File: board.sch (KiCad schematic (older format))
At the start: 48 parts, among them J1 H3, J2 USB-UART, J3 H2, J4 H1, J5 PWR, J6 DL, J7 H4, Q1 Q_NPN_BCE, Q2 Q_NPN_BCE, SW1 RESET, U1 ASSoC, U2 LM1117-3.3, U3 LM1117-3.3, Y1 25 MHz

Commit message: Fix crystal's capacitor value, voltage regulator value. Improve overall placement.
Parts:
- C18: value 18n -> 18p
- U2: value LM1117-3.3 -> LM1117-1.8; symbol Regulator_Linear:LM1117-3.3 -> Regulator_Linear:LM1117-1.8
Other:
- note added: "1.8V LED"
- note added: "3.3V LED"
- note added: "External Memory"
- note added: "Power Access"
- note added: "Test Mode"
- note removed: "Extra Power Access"
- note removed: "Power LED (1.8v)"
- note removed: "Power LED (3.3v)"
- note removed: "Test Mode Switches"
- moved on the sheet: C17, C18, C19, D1, D2, J1, J3, J4, J6, J7, JP1, Q1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

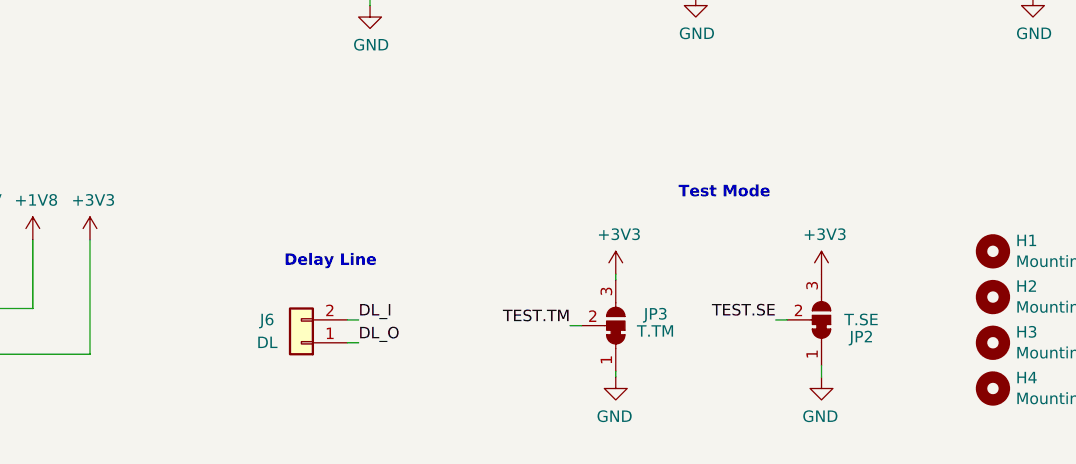
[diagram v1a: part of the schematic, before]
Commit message: Update using kicad 5.1.12
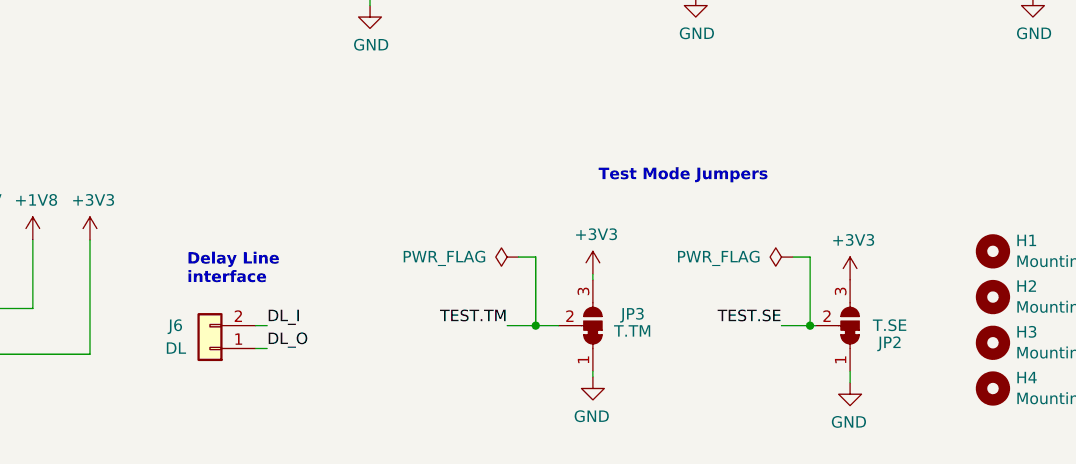
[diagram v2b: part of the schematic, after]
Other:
- note added: "Delay Line\ninterface"
- note added: "Test Mode Jumpers"
- note removed: "Delay Line"
- note removed: "Test Mode"
- moved on the sheet: J6, JP2, JP3
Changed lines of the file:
@@
 L Jumper:SolderJumper_3_Bridged12 JP3
 U 1 1 600FDD3B
-P 4450 7200
-F 0 "JP3" V 4500 7375 50  0000 C CNN
-F 1 "T.TM" V 4425 7375 50  0000 C CNN
-F 2 "Jumper:SolderJumper-3_P1.3mm_Bridged2Bar12_RoundedPad1.0x1.5mm" H 4450 7200 50  0001 C CNN
-F 3 "~" H 4450 7200 50  0001 C CNN
-	1    4450 7200
+P 4350 7200
+F 0 "JP3" V 4400 7375 50  0000 C CNN
+F 1 "T.TM" V 4325 7375 50  0000 C CNN
+F 2 "Jumper:SolderJumper-3_P1.3mm_Bridged2Bar12_RoundedPad1.0x1.5mm" H 4350 7200 50  0001 C CNN
+F 3 "~" H 4350 7200 50  0001 C CNN
+	1    4350 7200
 	0    1    -1   0
 $EndComp
@@
 L Jumper:SolderJumper_3_Bridged12 JP2
 U 1 1 6010189E
-P 5350 7175
-F 0 "JP2" V 5275 7350 50  0000 C CNN
-F 1 "T.SE" V 5350 7350 50  0000 C CNN
-F 2 "Jumper:SolderJumper-3_P1.3mm_Bridged2Bar12_RoundedPad1.0x1.5mm" H 5350 7175 50  0001 C CNN
-F 3 "~" H 5350 7175 50  0001 C CNN
-	1    5350 7175
+P 5475 7200
+F 0 "JP2" V 5400 7375 50  0000 C CNN
+F 1 "T.SE" V 5475 7375 50  0000 C CNN
+F 2 "Jumper:SolderJumper-3_P1.3mm_Bridged2Bar12_RoundedPad1.0x1.5mm" H 5475 7200 50  0001 C CNN
+F 3 "~" H 5475 7200 50  0001 C CNN
+	1    5475 7200
 	0    1    -1   0
 $EndComp
 Wire Wire Line
-	4450 7400 4450 7425
+	4350 7400 4350 7425
 $Comp
 L power:GND #PWR036
 U 1 1 60103E00
-P 4450 7425
-F 0 "#PWR036" H 4450 7175 50  0001 C CNN
-F 1 "GND" H 4455 7252 50  0000 C CNN
-F 2 "" H 4450 7425 50  0001 C CNN
-F 3 "" H 4450 7425 50  0001 C CNN
-	1    4450 7425
+P 4350 7425
+F 0 "#PWR036" H 4350 7175 50  0001 C CNN
+F 1 "GND" H 4355 7252 50  0000 C CNN
+F 2 "" H 4350 7425 50  0001 C CNN
+F 3 "" H 4350 7425 50  0001 C CNN
+	1    4350 7425
 	-1   0    0    -1
 $EndComp
@@
 L power:GND #PWR037
 U 1 1 6010E9C0
-P 5350 7425
-F 0 "#PWR037" H 5350 7175 50  0001 C CNN
-F 1 "GND" H 5355 7252 50  0000 C CNN
-F 2 "" H 5350 7425 50  0001 C CNN
-F 3 "" H 5350 7425 50  0001 C CNN
-	1    5350 7425
+P 5475 7450
+F 0 "#PWR037" H 5475 7200 50  0001 C CNN
+F 1 "GND" H 5480 7277 50  0000 C CNN
+F 2 "" H 5475 7450 50  0001 C CNN
+F 3 "" H 5475 7450 50  0001 C CNN
+	1    5475 7450
 	-1   0    0    -1
 $EndComp
@@
 L power:+3V3 #PWR034
 U 1 1 60137BAC
-P 4450 6975
-F 0 "#PWR034" H 4450 6825 50  0001 C CNN
-F 1 "+3V3" H 4465 7148 50  0000 C CNN
-F 2 "" H 4450 6975 50  0001 C CNN
-F 3 "" H 4450 6975 50  0001 C CNN
-	1    4450 6975
-	1    0    0    -1
-$EndComp
-Wire Wire Line
-	5350 7375 5350 7425
+P 4350 6975
+F 0 "#PWR034" H 4350 6825 50  0001 C CNN
+F 1 "+3V3" H 4365 7148 50  0000 C CNN
+F 2 "" H 4350 6975 50  0001 C CNN
+F 3 "" H 4350 6975 50  0001 C CNN
+	1    4350 6975
+	1    0    0    -1
+$EndComp
+Wire Wire Line
+	5475 7400 5475 7450
 $Comp
 L Connector_Generic:Conn_01x12 J1
@@
 L Connector_Generic:Conn_01x02 J6
 U 1 1 603C23F2
-P 3075 7275
-F 0 "J6" H 3225 7175 50  0000 C CNN
-F 1 "DL" H 3225 7275 50  0000 C CNN
-F 2 "Connector_PinSocket_2.54mm:PinSocket_1x02_P2.54mm_Vertical" H 3075 7275 50  0001 C CNN
-F 3 "~" H 3075 7275 50  0001 C CNN
-	1    3075 7275
+P 2675 7300
+F 0 "J6" H 2825 7200 50  0000 C CNN
+F 1 "DL" H 2825 7300 50  0000 C CNN
+F 2 "Connector_PinSocket_2.54mm:PinSocket_1x02_P2.54mm_Vertical" H 2675 7300 50  0001 C CNN
+F 3 "~" H 2675 7300 50  0001 C CNN
+	1    2675 7300
 	-1   0    0    1
 $EndComp
@@
 	8625 1475 8625 1525
 Wire Wire Line
-	4450 6975 4450 7000
+	4350 6975 4350 7000
 Text Label 9675 3075 0    50   ~ 0
 TEST.TM
@@
 L power:+3V3 #PWR035
 U 1 1 605DD584
-P 5350 6975
-F 0 "#PWR035" H 5350 6825 50  0001 C CNN
-F 1 "+3V3" H 5365 7148 50  0000 C CNN
-F 2 "" H 5350 6975 50  0001 C CNN
-F 3 "" H 5350 6975 50  0001 C CNN
-	1    5350 6975
+P 5475 7000
+F 0 "#PWR035" H 5475 6850 50  0001 C CNN
+F 1 "+3V3" H 5490 7173 50  0000 C CNN
+F 2 "" H 5475 7000 50  0001 C CNN
+F 3 "" H 5475 7000 50  0001 C CNN
+	1    5475 7000
 	1    0    0    -1
 $EndComp
@@
 Text Label 10625 5125 2    50   ~ 0
 A5
-Text Label 3325 7275 0    50   ~ 0
+Text Label 2925 7300 0    50   ~ 0
 DL_O
-Text Label 3325 7175 0    50   ~ 0
+Text Label 2925 7200 0    50   ~ 0
 DL_I
 Wire Wire Line
-	3325 7275 3275 7275
-Wire Wire Line
-	3325 7175 3275 7175
+	2925 7300 2875 7300
+Wire Wire Line
+	2925 7200 2875 7200
 $Comp
 L GAPH-Chips:ASSoC U1
@@
 Wire Wire Line
 	7150 3175 7275 3175
-Text Label 4250 7200 2    50   ~ 0
+Text Label 3975 7200 2    50   ~ 0
 TEST.TM
 Wire Wire Line
-	4250 7200 4300 7200
-Text Label 5150 7175 2    50   ~ 0
+	3975 7200 4100 7200
+Text Label 5175 7200 2    50   ~ 0
 TEST.SE
 Wire Wire Line
-	5150 7175 5200 7175
+	5175 7200 5300 7200
 Text Label 10625 4825 2    50   ~ 0
 ASSOC_TX
@@
 Wire Wire Line
 	7175 3675 7275 3675
-Text Notes 4725 6650 0    50   ~ 10
-Test Mode
-Text Notes 3000 6950 0    50   ~ 10
-Delay Line
+Text Notes 4375 6575 0    50   ~ 10
+Test Mode Jumpers
+Text Notes 2575 7025 0    50   ~ 10
+Delay Line\ninterface
 Text Notes 10650 1875 0    50   ~ 10
 GPIOs
@@
 Text Notes 10375 5650 0    50   ~ 10
 External Memory
+$Comp
+L power:PWR_FLAG #FLG0102
+U 1 1 61D4FB3D
+P 4025 6900
+F 0 "#FLG0102" H 4025 6975 50  0001 C CNN
+F 1 "PWR_FLAG" V 4025 7225 50  0000 C CNN
+F 2 "" H 4025 6900 50  0001 C CNN
+F 3 "~" H 4025 6900 50  0001 C CNN
+	1    4025 6900
+	0    -1   -1   0
+$EndComp
+Wire Wire Line
+	4025 6900 4100 6900
+Wire Wire Line
+	4100 6900 4100 7200
+Connection ~ 4100 7200
+Wire Wire Line
+	4100 7200 4200 7200
+$Comp
+L power:PWR_FLAG #FLG0103
+U 1 1 61D6E63E
+P 5225 6900
+F 0 "#FLG0103" H 5225 6975 50  0001 C CNN
+F 1 "PWR_FLAG" V 5225 7225 50  0000 C CNN
+F 2 "" H 5225 6900 50  0001 C CNN
+F 3 "~" H 5225 6900 50  0001 C CNN
+	1    5225 6900
+	0    -1   -1   0
+$EndComp
+Wire Wire Line
+	5225 6900 5300 6900
+Wire Wire Line
+	5300 6900 5300 7200
+Connection ~ 5300 7200
+Wire Wire Line
+	5300 7200 5325 7200
 $EndSCHEMATC
